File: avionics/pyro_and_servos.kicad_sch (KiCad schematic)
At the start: 16 parts, among them J3 PYRO_0, J4 Servo_0, J5 Servo_1, J6 Servo_2, J7 Servo_3, Q1 AO3400A, U6 74AHCT125

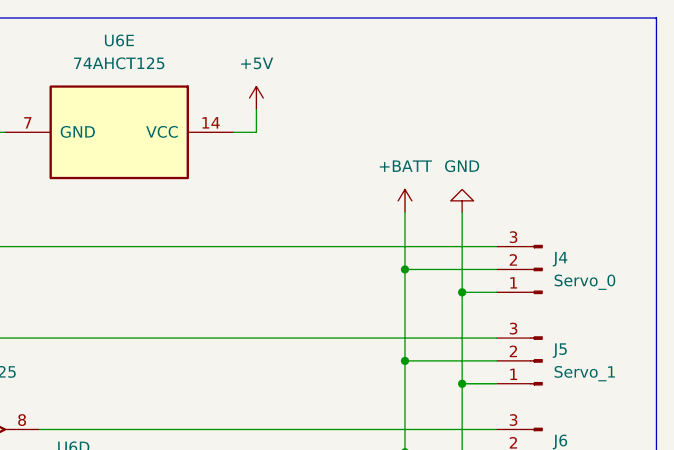
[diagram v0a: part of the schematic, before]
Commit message: Avionics: fixed improper power pin for servos
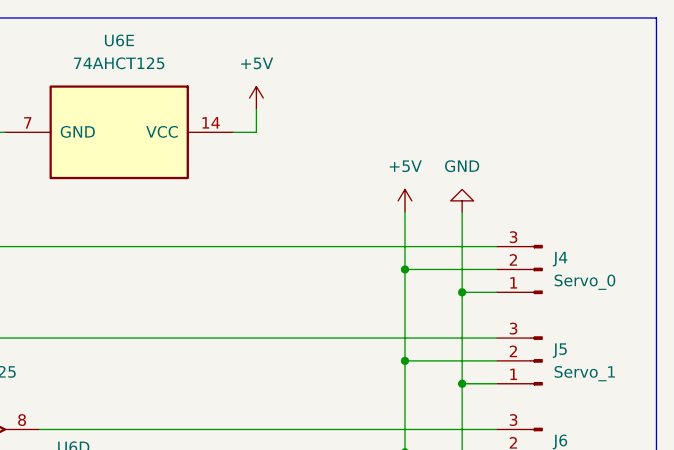
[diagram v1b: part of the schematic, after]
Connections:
- net +5V: now also J4.2 (Pin_2), J5.2 (Pin_2), J6.2 (Pin_2), J7.2 (Pin_2)
- net +BATT: no longer J4.2 (Pin_2), J5.2 (Pin_2), J6.2 (Pin_2), J7.2 (Pin_2)
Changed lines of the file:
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@@
+	)
+	(symbol
+		(lib_id "power:+5V")
+		(at 182.88 45.72 0)
+		(unit 1)
+		(exclude_from_sim no)
+		(in_bom yes)
+		(on_board yes)
+		(dnp no)
+		(fields_autoplaced yes)
+		(property "Reference" "#PWR031"
+			(at 182.88 49.53 0)
+			(effects
+				(font
+					(size 1.27 1.27)
+				)
+				(hide yes)
+			)
+		)
+		(property "Value" "+5V"
+			(at 182.88 40.64 0)
+			(effects
+				(font
+					(size 1.27 1.27)
+				)
+			)
+		)
+		(property "Footprint" ""
+			(at 182.88 45.72 0)
+			(effects
+				(font
+					(size 1.27 1.27)
+				)
+				(hide yes)
+			)
+		)
+		(property "Datasheet" ""
+			(at 182.88 45.72 0)
+			(effects
+				(font
+					(size 1.27 1.27)
+				)
+				(hide yes)
+			)
+		)
+		(property "Description" "Power symbol creates a global label with name \"+5V\""
+			(at 182.88 45.72 0)
+			(effects
+				(font
+					(size 1.27 1.27)
+				)
+				(hide yes)
+			)
+		)
+		(pin "1"
+		)
+		(instances
+			(project ""
+				(path "/5552e11b-fce5-44fd-aeb8-61bf7d07571f/9e1a8ef6-58a8-42c3-a8df-b8575642bd98"
+					(reference "#PWR031")
+					(unit 1)
+				)
+			)
+		)
 	)
 	(symbol
@@
 					(unit 1)
 				)
-			)
-		)
-	)
-	(symbol
-		(lib_id "power:+BATT")
-		(at 182.88 45.72 0)
-		(unit 1)
-		(exclude_from_sim no)
-		(in_bom yes)
-		(on_board yes)
-		(dnp no)
-		(fields_autoplaced yes)
-		(property "Reference" "#PWR031"
-			(at 182.88 49.53 0)
-			(effects
-				(font
-					(size 1.27 1.27)
-				)
-				(hide yes)
-			)
-		)
-		(property "Value" "+BATT"
-			(at 182.88 40.64 0)
-			(effects
-				(font
-					(size 1.27 1.27)
-				)
-			)
-		)
-		(property "Footprint" ""
-			(at 182.88 45.72 0)
-			(effects
-				(font
-					(size 1.27 1.27)
-				)
-				(hide yes)
-			)
-		)
-		(property "Datasheet" ""
-			(at 182.88 45.72 0)
-			(effects
-				(font
-					(size 1.27 1.27)
-				)
-				(hide yes)
-			)
-		)
-		(property "Description" "Power symbol creates a global label with name \"+BATT\""
-			(at 182.88 45.72 0)
-			(effects
-				(font
-					(size 1.27 1.27)
-				)
-				(hide yes)
-			)
-		)
-		(pin "1"
-		)
-		(instances
-			(project "avionics"
-				(path "/5552e11b-fce5-44fd-aeb8-61bf7d07571f/9e1a8ef6-58a8-42c3-a8df-b8575642bd98"
-					(reference "#PWR031")
-					(unit 1)
-				)

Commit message: created pcb, nearly done with traces, finalising for ordering soon
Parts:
- J3: footprint Connector_PinHeader_2.54mm:PinHeader_1x02_P2.54mm_Vertical -> TerminalBlock_Phoenix:TerminalBlock_Phoenix_MKDS-1,5-2_1x02_P5.00mm_Horizontal
- J4, J5, J6, J7: footprint Connector_PinHeader_2.54mm:PinHeader_1x03_P2.54mm_Vertical -> TerminalBlock_Phoenix:TerminalBlock_Phoenix_MKDS-1,5-3-5.08_1x03_P5.08mm_Horizontal
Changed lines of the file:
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@@
 			)
 		)
-		(property "Footprint" "Connector_PinHeader_2.54mm:PinHeader_1x03_P2.54mm_Vertical"
+		(property "Footprint" "TerminalBlock_Phoenix:TerminalBlock_Phoenix_MKDS-1,5-3-5.08_1x03_P5.08mm_Horizontal"
 			(at 198.12 82.55 0)
 			(effects
@@
 			)
 		)
-		(property "Footprint" "Connector_PinHeader_2.54mm:PinHeader_1x03_P2.54mm_Vertical"
+		(property "Footprint" "TerminalBlock_Phoenix:TerminalBlock_Phoenix_MKDS-1,5-3-5.08_1x03_P5.08mm_Horizontal"
 			(at 198.12 72.39 0)
 			(effects
@@
 			)
 		)
-		(property "Footprint" "Connector_PinHeader_2.54mm:PinHeader_1x02_P2.54mm_Vertical"
+		(property "Footprint" "TerminalBlock_Phoenix:TerminalBlock_Phoenix_MKDS-1,5-2_1x02_P5.00mm_Horizontal"
 			(at 166.37 119.38 0)
 			(effects
@@
 			)
 		)
-		(property "Footprint" "Connector_PinHeader_2.54mm:PinHeader_1x03_P2.54mm_Vertical"
+		(property "Footprint" "TerminalBlock_Phoenix:TerminalBlock_Phoenix_MKDS-1,5-3-5.08_1x03_P5.08mm_Horizontal"
 			(at 198.12 62.23 0)
 			(effects
@@
 			)
 		)
-		(property "Footprint" "Connector_PinHeader_2.54mm:PinHeader_1x03_P2.54mm_Vertical"
+		(property "Footprint" "TerminalBlock_Phoenix:TerminalBlock_Phoenix_MKDS-1,5-3-5.08_1x03_P5.08mm_Horizontal"
 			(at 198.12 52.07 0)
 			(effects

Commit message: hw: make board smaller, misc hotfixes
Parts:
- removed TP16: TP_SERVO_0, TestPoint:TestPoint_Pad_D1.5mm, symbol Connector:TestPoint
- removed TP17: TP_SERVO_1, TestPoint:TestPoint_Pad_D1.5mm, symbol Connector:TestPoint
- removed TP18: TP_SERVO_2, TestPoint:TestPoint_Pad_D1.5mm, symbol Connector:TestPoint
- removed TP19: TP_SERVO_3, TestPoint:TestPoint_Pad_D1.5mm, symbol Connector:TestPoint
- added J3: SW_ARM, TerminalBlock_Phoenix:TerminalBlock_Phoenix_MKDS-1,5-2_1x02_P5.00mm_Horizontal, symbol Connector:Conn_01x02_Pin
- R14: renamed from R10; footprint Resistor_SMD:R_0805_2012Metric_Pad1.20x1.40mm_HandSolder -> Resistor_SMD:R_0603_1608Metric
- R15: renamed from R11; footprint Resistor_SMD:R_0805_2012Metric_Pad1.20x1.40mm_HandSolder -> Resistor_SMD:R_0603_1608Metric
- R16: renamed from R12; footprint Resistor_SMD:R_0805_2012Metric_Pad1.20x1.40mm_HandSolder -> Resistor_SMD:R_0603_1608Metric
- R17: renamed from R13; footprint Resistor_SMD:R_0805_2012Metric_Pad1.20x1.40mm_HandSolder -> Resistor_SMD:R_0603_1608Metric
- renumbered J3 to J4, J4 to J5, J5 to J6, J6 to J7, J7 to J8, Q1 to Q2, TP20 to TP16
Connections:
- net +BATT: now also J3.1 (Pin_1); no longer J4.1 (Pin_1)
- new net: J3.2 (Pin_2), J4.1 (Pin_1)
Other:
- moved on the sheet: J4, Q2, R14, R15, R16, R17, TP16

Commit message: hw: order pcb
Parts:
- removed TP16: TP_PYRO_0, TestPoint:TestPoint_Pad_D1.5mm, symbol Connector:TestPoint
- added C18: 1u, Capacitor_SMD:C_0603_1608Metric, symbol Device:C
- added C19: 1000u, Capacitor_THT:CP_Radial_D10.0mm_P5.00mm, symbol Device:C_Polarized
- J2: renamed from J3; value SW_ARM -> 1x2_header; Mouser Part Number (none) -> 651-1711026
- J3: renamed from J4; value PYRO_0 -> 1x2_header; Mouser Part Number (none) -> 651-1711026
- J4: renamed from J5; value Servo_0 -> 1x3_header; footprint TerminalBlock_Phoenix:TerminalBlock_Phoenix_MKDS-1,5-3-5.08_1x03_P5.08mm_Horizontal -> Connector_PinHeader_2.54mm:PinHeader_1x03_P2.54mm_Vertical; Mouser Part Number (none) -> 538-22-23-6032
- J5: renamed from J6; value Servo_1 -> 1x3_header; footprint TerminalBlock_Phoenix:TerminalBlock_Phoenix_MKDS-1,5-3-5.08_1x03_P5.08mm_Horizontal -> Connector_PinHeader_2.54mm:PinHeader_1x03_P2.54mm_Vertical; Mouser Part Number (none) -> 538-22-23-6032
- J6: renamed from J7; value Servo_2 -> 1x3_header; footprint TerminalBlock_Phoenix:TerminalBlock_Phoenix_MKDS-1,5-3-5.08_1x03_P5.08mm_Horizontal -> Connector_PinHeader_2.54mm:PinHeader_1x03_P2.54mm_Vertical; Mouser Part Number (none) -> 538-22-23-6032
- J7: renamed from J8; value Servo_3 -> 1x3_header; footprint TerminalBlock_Phoenix:TerminalBlock_Phoenix_MKDS-1,5-3-5.08_1x03_P5.08mm_Horizontal -> Connector_PinHeader_2.54mm:PinHeader_1x03_P2.54mm_Vertical; Mouser Part Number (none) -> 538-22-23-6032
- Q2: DigiKey Part Number (none) -> 785-1000-1-ND; LCSC Part Number (none) -> C20917
- R18: renamed from R14; DigiKey Part Number (none) -> 311-100KHRCT-ND; Mouser Part Number (none) -> 594-MCT06030C1003FP5
- R19: renamed from R15; value 100 -> 33; DigiKey Part Number (none) -> 13-RC0603FR-0733RLCT-ND; Mouser Part Number (none) -> 710-560112116009
- R20: renamed from R16; DigiKey Part Number (none) -> 541-56.0KHCT-ND; Mouser Part Number (none) -> 603-RT0603FRE1356KL
- R21: renamed from R17; DigiKey Part Number (none) -> 311-33.0KHRCT-ND; Mouser Part Number (none) -> 71-TNPW060333K0BEEA
- U6: DigiKey Part Number (none) -> 296-4652-1-ND; LCSC Part Number (none) -> C155176
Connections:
- net +5V: now also C18.1, C19.1
- net GND: now also C18.2, C19.2
- net SERVO_1: now reaches J5.3 (Pin_3), U6.6
- net PYRO_0_Vout: now reaches J3.2 (Pin_2), Q2.3 (D), R20.1
- net SERVO_3: now reaches J7.3 (Pin_3), U6.11
- net SERVO_2: now reaches J6.3 (Pin_3), U6.8
- net PYRO_0_GATE: now reaches Q2.1 (G), R19.1
- net ARM_Vout: now reaches J2.2 (Pin_2), J3.1 (Pin_1)
- net SERVO_0: now reaches J4.3 (Pin_3), U6.3
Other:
- moved on the sheet: J2, J3, R18, R19
